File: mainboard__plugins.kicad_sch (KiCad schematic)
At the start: 7 parts

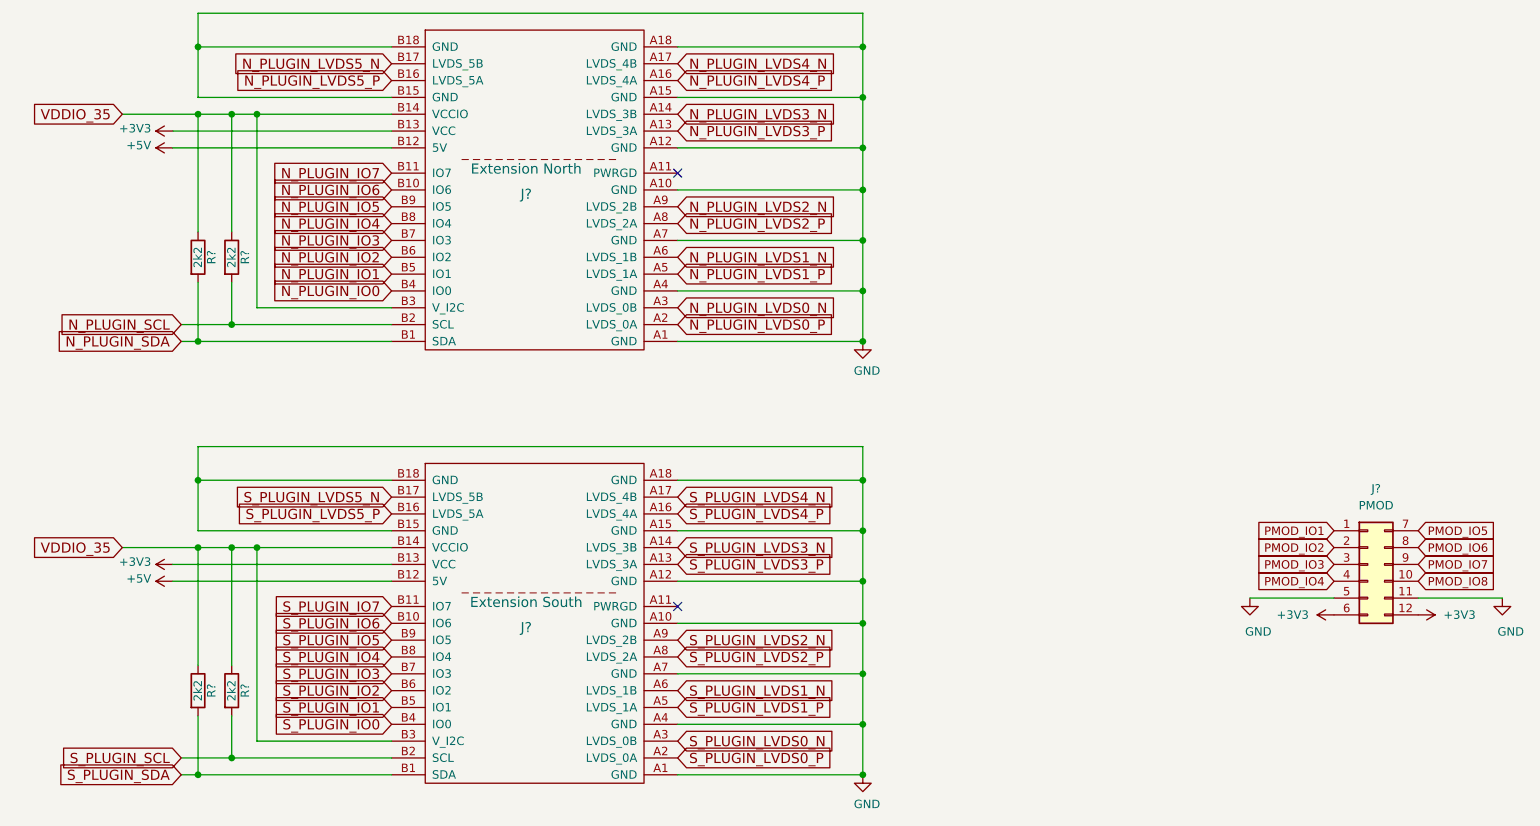
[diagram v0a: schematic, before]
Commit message: small tweaks; add mipi termination
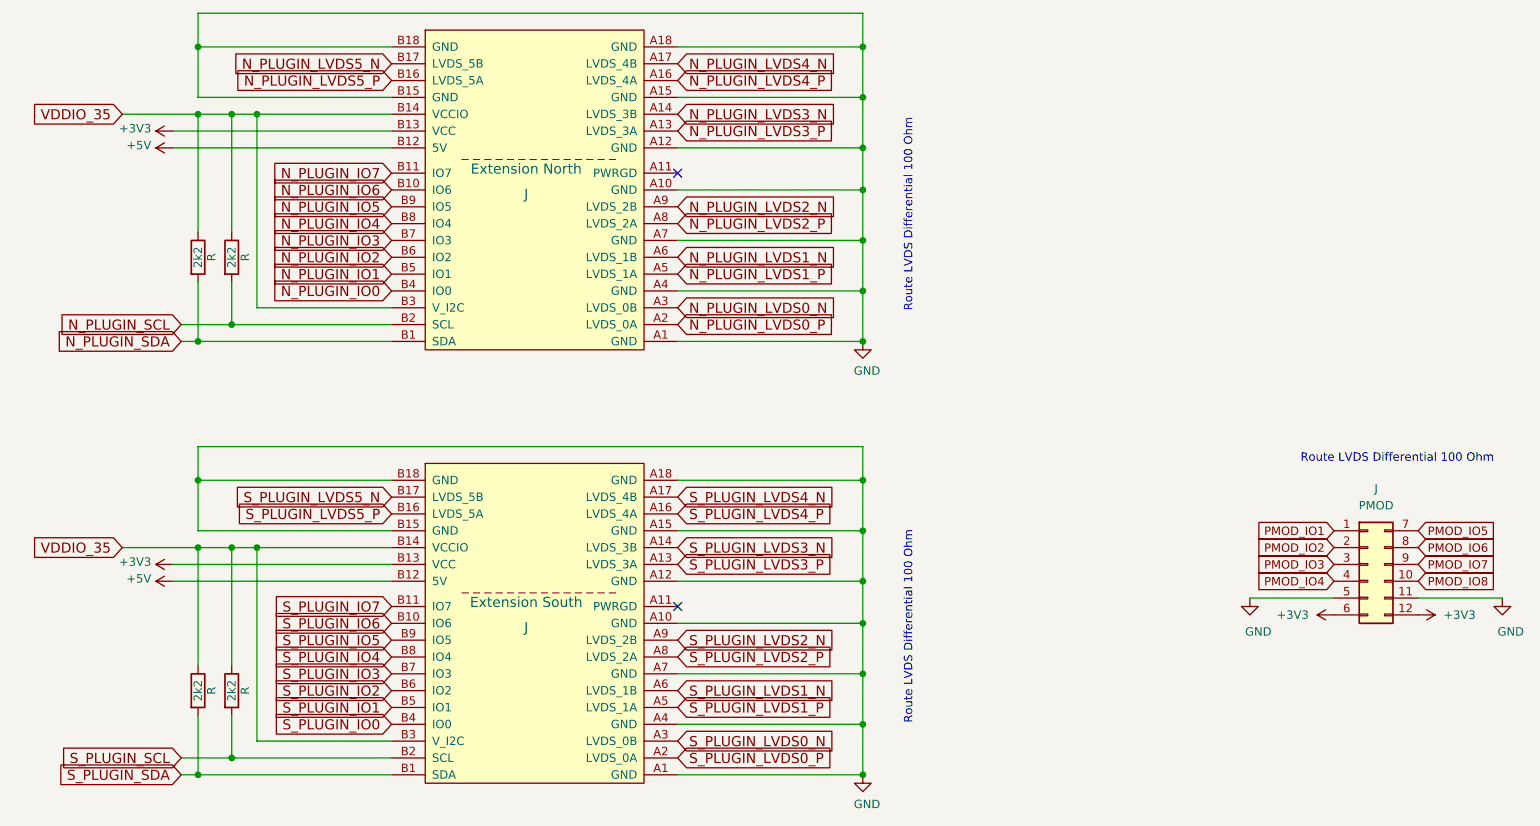
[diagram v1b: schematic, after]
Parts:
- gave numbers to parts that had none: 2
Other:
- note added: "Route LVDS Differential 100 Ohm"
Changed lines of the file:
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@@
     (stroke (width 0) (type solid) (color 0 0 0 0))
+  )
+  (text "Route LVDS Differential 100 Ohm" (at 165.1 88.9 90)
+    (effects (font (size 1.27 1.27)) (justify left bottom))
+  )
+  (text "Route LVDS Differential 100 Ohm" (at 165.1 151.13 90)
+    (effects (font (size 1.27 1.27)) (justify left bottom))
+  )
+  (text "Route LVDS Differential 100 Ohm" (at 252.73 111.76 180)
+    (effects (font (size 1.27 1.27)) (justify right bottom))
   )
   (global_label "VDDIO_35" (shape input) (at 45.72 59.055 180)    (property "Intersheet References" "${INTERSHEET_REFS}" (id 0) (at 30.255 58.9598 0)
@@
   (symbol (lib_id "power:+3V3") (at 53.34 61.595 90) (unit 1)
     (in_bom yes) (on_board yes)
-    (property "Reference" "#PWR?" (id 0) (at 57.15 61.595 0)
+    (property "Reference" "#PWR" (id 0) (at 57.15 61.595 0)
       (effects (font (size 1.27 1.27)) hide)
     )
@@
   (symbol (lib_id "power:+5V") (at 53.34 64.135 90) (unit 1)
     (in_bom yes) (on_board yes)
-    (property "Reference" "#PWR?" (id 0) (at 57.15 64.135 0)
+    (property "Reference" "#PWR" (id 0) (at 57.15 64.135 0)
       (effects (font (size 1.27 1.27)) hide)
     )
@@
   (symbol (lib_id "power:+3V3") (at 53.34 127 90) (unit 1)
     (in_bom yes) (on_board yes)
-    (property "Reference" "#PWR?" (id 0) (at 57.15 127 0)
+    (property "Reference" "#PWR" (id 0) (at 57.15 127 0)
       (effects (font (size 1.27 1.27)) hide)
     )
@@
   (symbol (lib_id "power:+5V") (at 53.34 129.54 90) (unit 1)
     (in_bom yes) (on_board yes)
-    (property "Reference" "#PWR?" (id 0) (at 57.15 129.54 0)
+    (property "Reference" "#PWR" (id 0) (at 57.15 129.54 0)
       (effects (font (size 1.27 1.27)) hide)
     )
@@
   (symbol (lib_id "power:+3V3") (at 228.6 134.62 90) (unit 1)
     (in_bom yes) (on_board yes)
-    (property "Reference" "#PWR?" (id 0) (at 232.41 134.62 0)
+    (property "Reference" "#PWR" (id 0) (at 232.41 134.62 0)
       (effects (font (size 1.27 1.27)) hide)
     )
@@
   (symbol (lib_id "power:+3V3") (at 241.3 134.62 270) (unit 1)
     (in_bom yes) (on_board yes)
-    (property "Reference" "#PWR?" (id 0) (at 237.49 134.62 0)
+    (property "Reference" "#PWR" (id 0) (at 237.49 134.62 0)
       (effects (font (size 1.27 1.27)) hide)
     )
@@
   (symbol (lib_id "power:GND") (at 157.48 93.345 0) (unit 1)
     (in_bom yes) (on_board yes)
-    (property "Reference" "#PWR?" (id 0) (at 157.48 99.695 0)
+    (property "Reference" "#PWR" (id 0) (at 157.48 99.695 0)
       (effects (font (size 1.27 1.27)) hide)
     )
@@
   (symbol (lib_id "power:GND") (at 157.48 158.75 0) (unit 1)
     (in_bom yes) (on_board yes)
-    (property "Reference" "#PWR?" (id 0) (at 157.48 165.1 0)
+    (property "Reference" "#PWR" (id 0) (at 157.48 165.1 0)
       (effects (font (size 1.27 1.27)) hide)
     )
@@
   (symbol (lib_id "power:GND") (at 215.9 132.08 0) (unit 1)
     (in_bom yes) (on_board yes)
-    (property "Reference" "#PWR?" (id 0) (at 215.9 138.43 0)
+    (property "Reference" "#PWR" (id 0) (at 215.9 138.43 0)
       (effects (font (size 1.27 1.27)) hide)
     )
@@
   (symbol (lib_id "power:GND") (at 254 132.08 0) (unit 1)
     (in_bom yes) (on_board yes)
-    (property "Reference" "#PWR?" (id 0) (at 254 138.43 0)
+    (property "Reference" "#PWR" (id 0) (at 254 138.43 0)
       (effects (font (size 1.27 1.27)) hide)
     )
@@
   (symbol (lib_id "Device:R") (at 57.15 80.645 0) (unit 1)
     (in_bom yes) (on_board yes)
-    (property "Reference" "R?" (id 0) (at 59.182 80.645 90))
+    (property "Reference" "R" (id 0) (at 59.182 80.645 90))
     (property "Value" "2k2" (id 1) (at 57.15 80.645 90))
     (property "Footprint" "Resistors_SMD:R_0603_HandSoldering" (id 2) (at 55.372 80.645 90)
       (effects (font (size 1.27 1.27)) hide)
     )
-    (property "Datasheet" "" (id 3) (at 57.15 80.645 0)
+    (property "Datasheet" "~" (id 3) (at 57.15 80.645 0)
       (effects (font (size 1.27 1.27)) hide)
     )
@@
   (symbol (lib_id "Device:R") (at 57.15 146.05 0) (unit 1)
     (in_bom yes) (on_board yes)
-    (property "Reference" "R?" (id 0) (at 59.182 146.05 90))
+    (property "Reference" "R" (id 0) (at 59.182 146.05 90))
     (property "Value" "2k2" (id 1) (at 57.15 146.05 90))
     (property "Footprint" "Resistors_SMD:R_0603_HandSoldering" (id 2) (at 55.372 146.05 90)
       (effects (font (size 1.27 1.27)) hide)
     )
-    (property "Datasheet" "" (id 3) (at 57.15 146.05 0)
+    (property "Datasheet" "~" (id 3) (at 57.15 146.05 0)
       (effects (font (size 1.27 1.27)) hide)
     )
@@
   (symbol (lib_id "Device:R") (at 62.23 80.645 0) (unit 1)
     (in_bom yes) (on_board yes)
-    (property "Reference" "R?" (id 0) (at 64.262 80.645 90))
+    (property "Reference" "R" (id 0) (at 64.262 80.645 90))
     (property "Value" "2k2" (id 1) (at 62.23 80.645 90))
     (property "Footprint" "Resistors_SMD:R_0603_HandSoldering" (id 2) (at 60.452 80.645 90)
       (effects (font (size 1.27 1.27)) hide)
     )
-    (property "Datasheet" "" (id 3) (at 62.23 80.645 0)
+    (property "Datasheet" "~" (id 3) (at 62.23 80.645 0)
       (effects (font (size 1.27 1.27)) hide)
     )
@@
   (symbol (lib_id "Device:R") (at 62.23 146.05 0) (unit 1)
     (in_bom yes) (on_board yes)
-    (property "Reference" "R?" (id 0) (at 64.262 146.05 90))
+    (property "Reference" "R" (id 0) (at 64.262 146.05 90))
     (property "Value" "2k2" (id 1) (at 62.23 146.05 90))
     (property "Footprint" "Resistors_SMD:R_0603_HandSoldering" (id 2) (at 60.452 146.05 90)
       (effects (font (size 1.27 1.27)) hide)
     )
-    (property "Datasheet" "" (id 3) (at 62.23 146.05 0)
+    (property "Datasheet" "~" (id 3) (at 62.23 146.05 0)
       (effects (font (size 1.27 1.27)) hide)
     )
@@
   (symbol (lib_id "Connector_Generic:Conn_02x06_Top_Bottom") (at 233.68 127 0) (unit 1)
     (in_bom yes) (on_board yes)
-    (property "Reference" "J?" (id 0) (at 234.95 115.57 0))
+    (property "Reference" "J" (id 0) (at 234.95 115.57 0))
     (property "Value" "PMOD" (id 1) (at 234.95 118.11 0))
     (property "Footprint" "" (id 2) (at 233.68 127 0)
@@
   (symbol (lib_id "pcie-36-axiom:PCIe-36-Axiom") (at 107.95 71.755 0) (unit 1)
     (in_bom yes) (on_board yes)
-    (property "Reference" "J?" (id 0) (at 106.68 71.12 0)
+    (property "Reference" "J" (id 0) (at 106.68 71.12 0)
       (effects (font (size 1.524 1.524)))
     )
@@
   (symbol (lib_name "pcie-36-axiom:PCIe-36-Axiom_1") (lib_id "pcie-36-axiom:PCIe-36-Axiom") (at 107.95 137.16 0) (unit 1)
     (in_bom yes) (on_board yes)
-    (property "Reference" "J?" (id 0) (at 106.68 136.525 0)
+    (property "Reference" "J" (id 0) (at 106.68 136.525 0)
       (effects (font (size 1.524 1.524)))
     )
